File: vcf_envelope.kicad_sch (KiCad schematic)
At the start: 19 parts, among them Q2 BC237, U15 4066, U8 4001, U9 Opamp_Dual

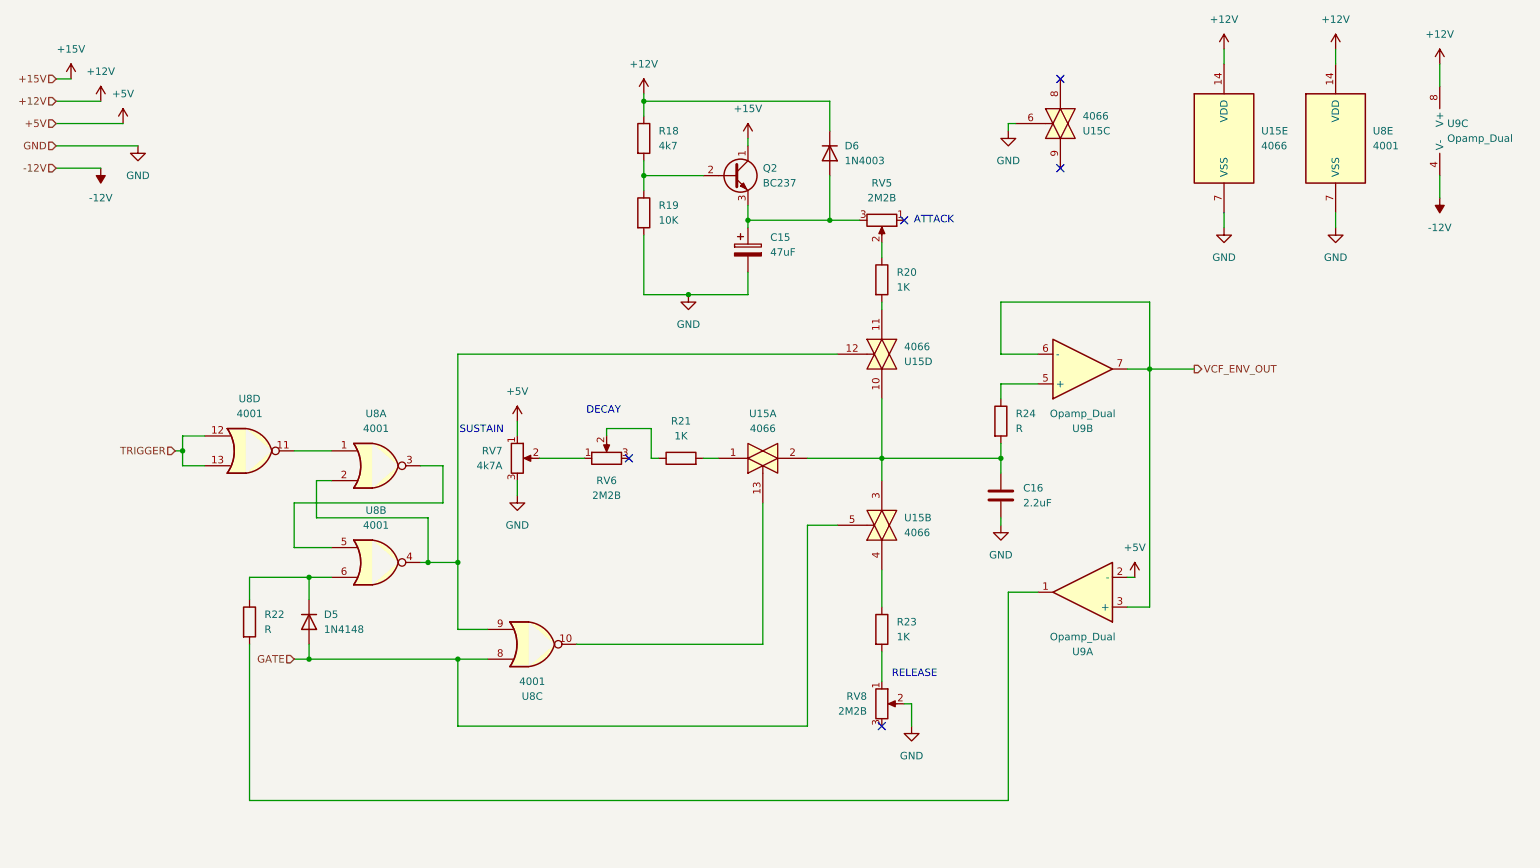
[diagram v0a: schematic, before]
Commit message: Add missing values and connectors
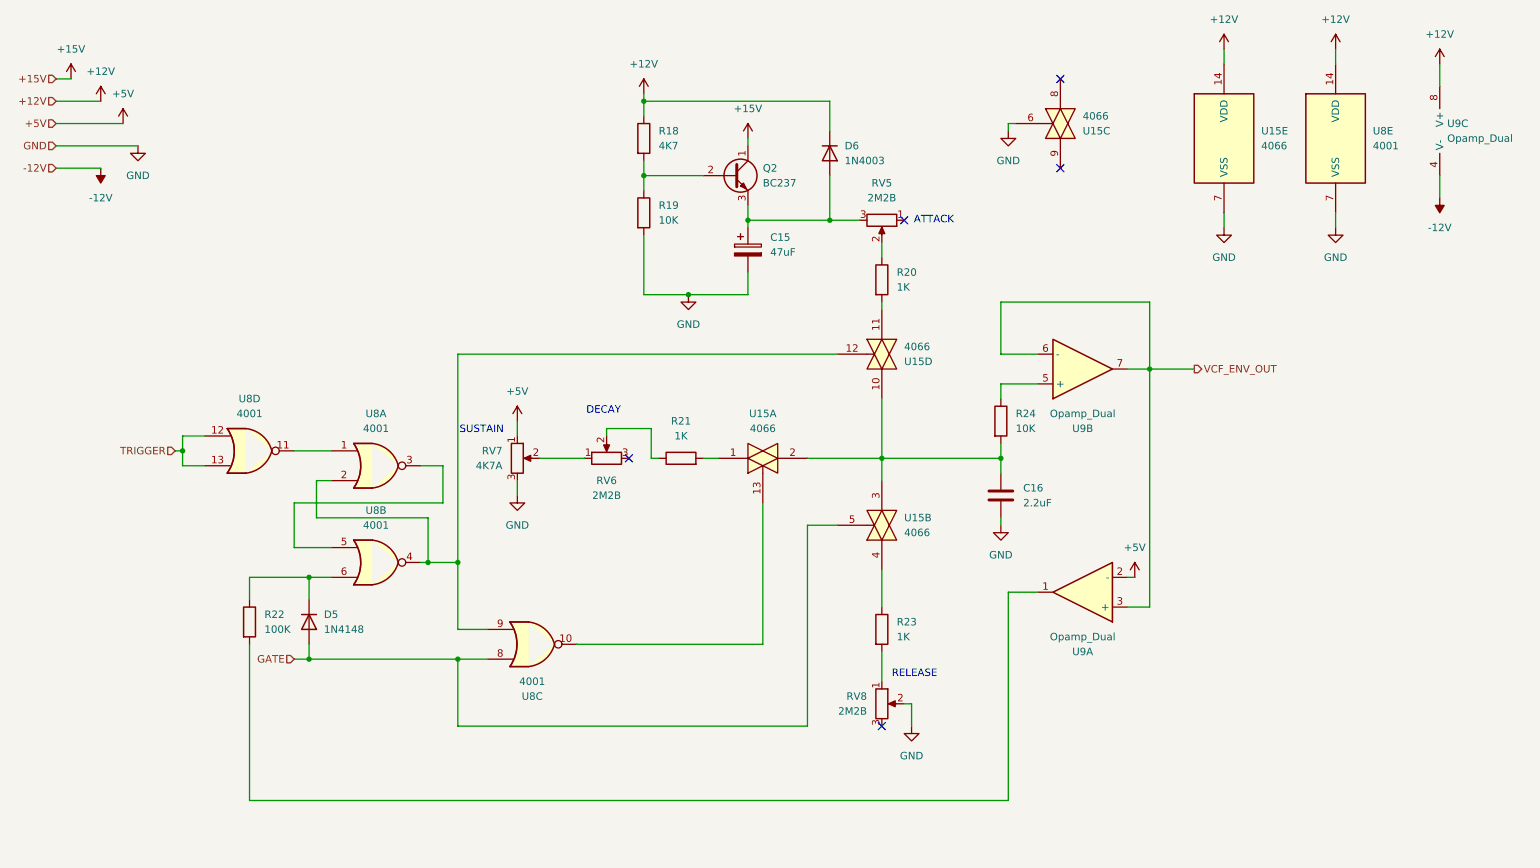
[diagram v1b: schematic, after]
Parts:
- R18: value 4k7 -> 4K7
- R22: value R -> 100K
- R24: value R -> 10K
- RV7: value 4k7A -> 4K7A
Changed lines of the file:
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@@
 			)
 		)
-		(property "Value" "R"
+		(property "Value" "100K"
 			(at 66.04 128.2699 0)
 			(effects
@@
 			)
 		)
-		(property "Value" "4k7"
+		(property "Value" "4K7"
 			(at 133.35 45.7199 0)
 			(effects
@@
 			)
 		)
-		(property "Value" "R"
+		(property "Value" "10K"
 			(at 194.31 93.9799 0)
 			(effects
@@
 			)
 		)
-		(property "Value" "4k7A"
+		(property "Value" "4K7A"
 			(at 106.68 100.3299 0)
 			(effects

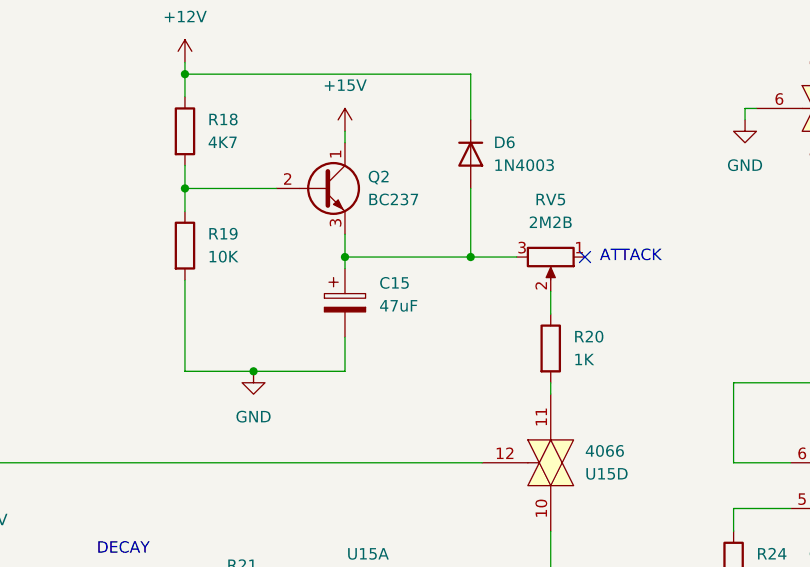
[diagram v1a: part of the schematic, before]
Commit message: Assign footprints and start PCB
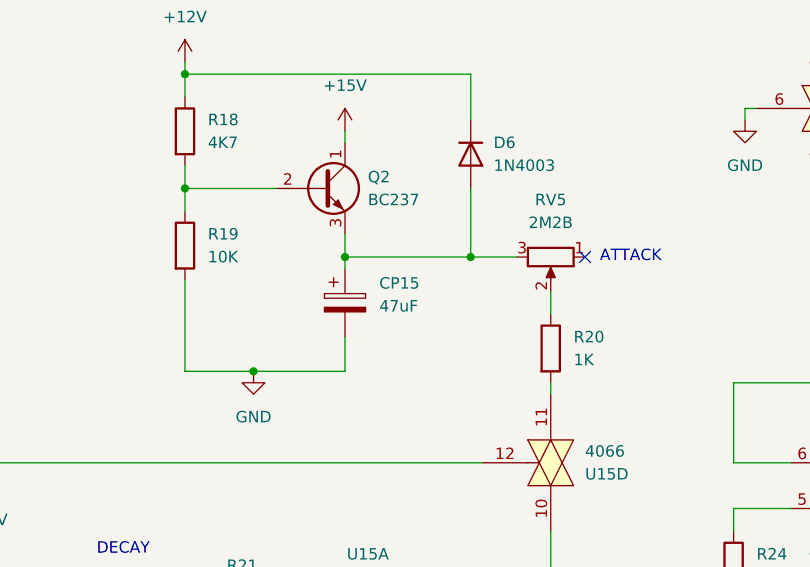
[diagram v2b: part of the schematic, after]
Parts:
- C16: footprint (none) -> Capacitor_THT:C_Disc_D5.0mm_W2.5mm_P5.00mm
- CP15: renamed from C15; footprint (none) -> Capacitor_THT:CP_Radial_D8.0mm_P3.80mm
- R18, R19, R20, R21, R22, R23, R24: footprint (none) -> Resistor_THT:R_Axial_DIN0204_L3.6mm_D1.6mm_P7.62mm_Horizontal
- RV5, RV6, RV7, RV8: footprint (none) -> Potentiometer_THT:Potentiometer_Omeg_PC16BU_Vertical
- U15: footprint (none) -> Package_DIP:DIP-14_W7.62mm_LongPads
- U8: footprint (none) -> Package_DIP:DIP-16_W7.62mm_LongPads
- U9: footprint (none) -> Package_DIP:DIP-8_W7.62mm_LongPads
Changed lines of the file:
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@@
 			)
 		)
-		(property "Footprint" ""
+		(property "Footprint" "Resistor_THT:R_Axial_DIN0204_L3.6mm_D1.6mm_P7.62mm_Horizontal"
 			(at 129.032 57.15 90)
 			(effects
@@
 			)
 		)
-		(property "Footprint" ""
+		(property "Footprint" "Resistor_THT:R_Axial_DIN0204_L3.6mm_D1.6mm_P7.62mm_Horizontal"
 			(at 61.722 127 90)
 			(effects
@@
 			)
 		)
-		(property "Footprint" ""
+		(property "Footprint" "Resistor_THT:R_Axial_DIN0204_L3.6mm_D1.6mm_P7.62mm_Horizontal"
 			(at 129.032 44.45 90)
 			(effects
@@
 			)
 		)
-		(property "Footprint" ""
+		(property "Footprint" "Package_DIP:DIP-8_W7.62mm_LongPads"
 			(at 205.74 83.82 0)
 			(effects
@@
 			)
 		)
-		(property "Footprint" ""
+		(property "Footprint" "Package_DIP:DIP-14_W7.62mm_LongPads"
 			(at 171.45 110.49 0)
 			(effects
@@
 			)
 		)
-		(property "Footprint" ""
+		(property "Footprint" "Package_DIP:DIP-14_W7.62mm_LongPads"
 			(at 201.93 41.91 0)
 			(effects
@@
 			)
 		)
-		(property "Footprint" ""
+		(property "Footprint" "Capacitor_THT:C_Disc_D5.0mm_W2.5mm_P5.00mm"
 			(at 190.8048 101.6 0)
 			(effects
@@
 			)
 		)
-		(property "Footprint" ""
+		(property "Footprint" "Resistor_THT:R_Axial_DIN0204_L3.6mm_D1.6mm_P7.62mm_Horizontal"
 			(at 137.16 100.838 90)
 			(effects
@@
 			)
 		)
-		(property "Footprint" ""
+		(property "Footprint" "Package_DIP:DIP-14_W7.62mm_LongPads"
 			(at 151.13 99.06 0)
 			(effects
@@
 			)
 		)
-		(property "Footprint" ""
+		(property "Footprint" "Potentiometer_THT:Potentiometer_Omeg_PC16BU_Vertical"
 			(at 171.45 58.42 0)
 			(effects
@@
 			)
 		)
-		(property "Footprint" ""
+		(property "Footprint" "Resistor_THT:R_Axial_DIN0204_L3.6mm_D1.6mm_P7.62mm_Horizontal"
 			(at 189.992 92.71 90)
 			(effects
@@
 			)
 		)
-		(property "Footprint" ""
+		(property "Footprint" "Package_DIP:DIP-14_W7.62mm_LongPads"
 			(at 229.87 44.45 0)
 			(effects
@@
 			)
 		)
-		(property "Footprint" ""
+		(property "Footprint" "Potentiometer_THT:Potentiometer_Omeg_PC16BU_Vertical"
 			(at 124.46 99.06 0)
 			(effects
@@
 			)
 		)
-		(property "Footprint" ""
+		(property "Footprint" "Package_DIP:DIP-8_W7.62mm_LongPads"
 			(at 205.74 121.92 0)
 			(effects
@@
 		(dnp no)
 		(fields_autoplaced yes)
-		(property "Reference" "C15"
+		(property "Reference" "CP15"
 			(at 152.4 61.3409 0)
 			(effects
@@
 			)
 		)
-		(property "Footprint" ""
+		(property "Footprint" "Capacitor_THT:CP_Radial_D8.0mm_P3.80mm"
 			(at 149.5552 67.31 0)
 			(effects
@@
 			(project "jensx1000"
 				(path "/3c53febc-5769-4c45-8f8f-0aba2c04e944/0274eb93-a765-4aec-bd65-1454f6ff4ea9"
-					(reference "C15")
+					(reference "CP15")
 					(unit 1)
 				)
@@
 			)
 		)
-		(property "Footprint" ""
+		(property "Footprint" "Package_DIP:DIP-8_W7.62mm_LongPads"
 			(at 269.24 43.18 0)
 			(effects
@@
 			)
 		)
-		(property "Footprint" ""
+		(property "Footprint" "Package_DIP:DIP-16_W7.62mm_LongPads"
 			(at 85.09 100.33 0)
 			(effects
@@
 			)
 		)
-		(property "Footprint" ""
+		(property "Footprint" "Package_DIP:DIP-16_W7.62mm_LongPads"
 			(at 248.92 44.45 0)
 			(effects
@@
 			)
 		)
-		(property "Footprint" ""
+		(property "Footprint" "Package_DIP:DIP-16_W7.62mm_LongPads"
 			(at 63.5 97.79 0)
 			(effects
@@
 			)
 		)
-		(property "Footprint" ""
+		(property "Footprint" "Resistor_THT:R_Axial_DIN0204_L3.6mm_D1.6mm_P7.62mm_Horizontal"
 			(at 169.672 128.27 90)
 			(effects
@@
 			)
 		)
-		(property "Footprint" ""
+		(property "Footprint" "Package_DIP:DIP-14_W7.62mm_LongPads"
 			(at 171.45 81.28 0)
 			(effects
@@
 			)
 		)
-		(property "Footprint" ""
+		(property "Footprint" "Package_DIP:DIP-16_W7.62mm_LongPads"
 			(at 111.76 130.81 0)
 			(effects
@@
 			)
 		)
-		(property "Footprint" ""
+		(property "Footprint" "Resistor_THT:R_Axial_DIN0204_L3.6mm_D1.6mm_P7.62mm_Horizontal"
 			(at 169.672 68.58 90)
 			(effects
@@
 			)
 		)
-		(property "Footprint" ""
+		(property "Footprint" "Potentiometer_THT:Potentiometer_Omeg_PC16BU_Vertical"
 			(at 171.45 140.97 0)
 			(effects
@@
 			)
 		)
-		(property "Footprint" ""
+		(property "Footprint" "Package_DIP:DIP-16_W7.62mm_LongPads"
 			(at 85.09 116.84 0)
 			(effects
@@
 			)
 		)
-		(property "Footprint" ""
+		(property "Footprint" "Potentiometer_THT:Potentiometer_Omeg_PC16BU_Vertical"
 			(at 109.22 99.06 0)
 			(effects

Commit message: VCF components are in position (but PCB size is wrong)
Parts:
- Q2: footprint Package_TO_SOT_THT:TO-92_Inline -> Package_TO_SOT_THT:TO-92_Inline_Wide
- R18, R19, R20, R21, R22, R23, R24: footprint Resistor_THT:R_Axial_DIN0204_L3.6mm_D1.6mm_P7.62mm_Horizontal -> Resistor_THT:R_Axial_DIN0207_L6.3mm_D2.5mm_P15.24mm_Horizontal
- U8: footprint Package_DIP:DIP-16_W7.62mm_LongPads -> Package_DIP:DIP-14_W7.62mm_Socket_LongPads
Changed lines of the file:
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@@
 			)
 		)
-		(property "Footprint" "Resistor_THT:R_Axial_DIN0204_L3.6mm_D1.6mm_P7.62mm_Horizontal"
+		(property "Footprint" "Resistor_THT:R_Axial_DIN0207_L6.3mm_D2.5mm_P15.24mm_Horizontal"
 			(at 129.032 57.15 90)
 			(effects
@@
 			)
 		)
-		(property "Footprint" "Resistor_THT:R_Axial_DIN0204_L3.6mm_D1.6mm_P7.62mm_Horizontal"
+		(property "Footprint" "Resistor_THT:R_Axial_DIN0207_L6.3mm_D2.5mm_P15.24mm_Horizontal"
 			(at 61.722 127 90)
 			(effects
@@
 			)
 		)
-		(property "Footprint" "Resistor_THT:R_Axial_DIN0204_L3.6mm_D1.6mm_P7.62mm_Horizontal"
+		(property "Footprint" "Resistor_THT:R_Axial_DIN0207_L6.3mm_D2.5mm_P15.24mm_Horizontal"
 			(at 129.032 44.45 90)
 			(effects
@@
 			)
 		)
-		(property "Footprint" "Resistor_THT:R_Axial_DIN0204_L3.6mm_D1.6mm_P7.62mm_Horizontal"
+		(property "Footprint" "Resistor_THT:R_Axial_DIN0207_L6.3mm_D2.5mm_P15.24mm_Horizontal"
 			(at 137.16 100.838 90)
 			(effects
@@
 			)
 		)
-		(property "Footprint" "Resistor_THT:R_Axial_DIN0204_L3.6mm_D1.6mm_P7.62mm_Horizontal"
+		(property "Footprint" "Resistor_THT:R_Axial_DIN0207_L6.3mm_D2.5mm_P15.24mm_Horizontal"
 			(at 189.992 92.71 90)
 			(effects
@@
 			)
 		)
-		(property "Footprint" "Package_DIP:DIP-16_W7.62mm_LongPads"
+		(property "Footprint" "Package_DIP:DIP-14_W7.62mm_Socket_LongPads"
 			(at 85.09 100.33 0)
 			(effects
@@
 			)
 		)
-		(property "Footprint" "Package_DIP:DIP-16_W7.62mm_LongPads"
+		(property "Footprint" "Package_DIP:DIP-14_W7.62mm_Socket_LongPads"
 			(at 248.92 44.45 0)
 			(effects
@@
 			)
 		)
-		(property "Footprint" "Package_DIP:DIP-16_W7.62mm_LongPads"
+		(property "Footprint" "Package_DIP:DIP-14_W7.62mm_Socket_LongPads"
 			(at 63.5 97.79 0)
 			(effects
@@
 			)
 		)
-		(property "Footprint" "Resistor_THT:R_Axial_DIN0204_L3.6mm_D1.6mm_P7.62mm_Horizontal"
+		(property "Footprint" "Resistor_THT:R_Axial_DIN0207_L6.3mm_D2.5mm_P15.24mm_Horizontal"
 			(at 169.672 128.27 90)
 			(effects
@@
 			)
 		)
-		(property "Footprint" "Package_DIP:DIP-16_W7.62mm_LongPads"
+		(property "Footprint" "Package_DIP:DIP-14_W7.62mm_Socket_LongPads"
 			(at 111.76 130.81 0)
 			(effects
@@
 			)
 		)
-		(property "Footprint" "Resistor_THT:R_Axial_DIN0204_L3.6mm_D1.6mm_P7.62mm_Horizontal"
+		(property "Footprint" "Resistor_THT:R_Axial_DIN0207_L6.3mm_D2.5mm_P15.24mm_Horizontal"
 			(at 169.672 68.58 90)
 			(effects
@@
 			)
 		)
-		(property "Footprint" "Package_DIP:DIP-16_W7.62mm_LongPads"
+		(property "Footprint" "Package_DIP:DIP-14_W7.62mm_Socket_LongPads"
 			(at 85.09 116.84 0)
 			(effects
@@
 			)
 		)
-		(property "Footprint" "Package_TO_SOT_THT:TO-92_Inline"
+		(property "Footprint" "Package_TO_SOT_THT:TO-92_Inline_Wide"
 			(at 151.13 52.705 0)
 			(effects

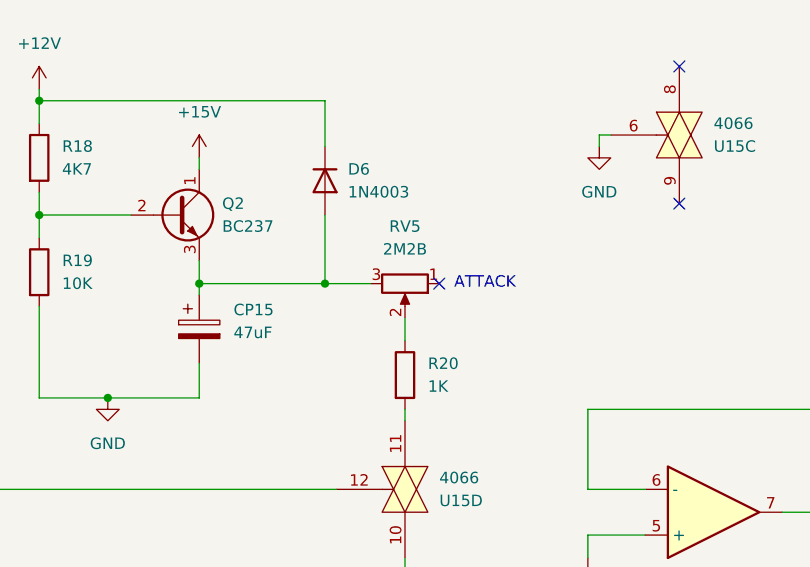
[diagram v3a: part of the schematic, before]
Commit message: Fix PCB sizes, adjust layout to new size
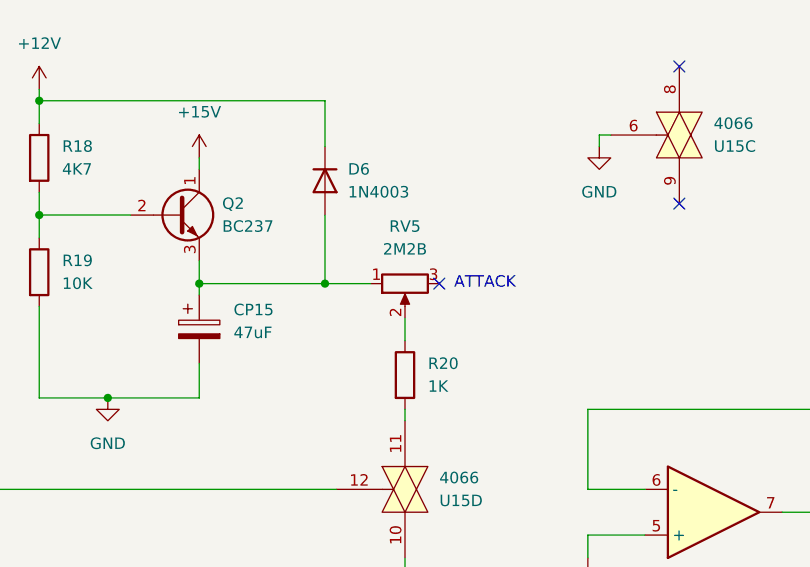
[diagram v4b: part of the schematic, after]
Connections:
- net at RV5.1: now also CP15.1, D6.2 (A), Q2.3 (E)
- now unconnected: RV5.3
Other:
- moved on the sheet: RV5
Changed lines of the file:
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@@
 	(symbol
 		(lib_id "Device:R_Potentiometer")
-		(at 171.45 58.42 270)
+		(at 171.45 58.42 90)
+		(mirror x)
 		(unit 1)
 		(exclude_from_sim no)
@@
 		(on_board yes)
 		(dnp no)
-		(fields_autoplaced yes)
 		(property "Reference" "RV5"
 			(at 171.45 52.07 90)

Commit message: Routing
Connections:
- net GND: now also R23.2; no longer RV8.2
- net at U15.4: now also RV8.1; no longer R23.1
- new net: R23.1, RV8.2
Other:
- moved on the sheet: R23, RV8
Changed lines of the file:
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@@
 	(text "RELEASE"
 		(exclude_from_sim no)
-		(at 177.038 135.89 0)
+		(at 166.624 134.366 0)
 		(effects
 			(font
@@
 	)
 	(junction
+		(at 176.53 140.97)
+		(diameter 0)
+		(color 0 0 0 0)
+	)
+	(junction
 		(at 52.07 97.79)
 		(diameter 0)
@@
 	)
 	(no_connect
-		(at 171.45 144.78)
+		(at 171.45 132.08)
 	)
 	(no_connect
@@
 	(wire
 		(pts
+			(xy 176.53 128.27) (xy 175.26 128.27)
+		)
+		(stroke
+			(width 0)
+			(type default)
+		)
+	)
+	(wire
+		(pts
 			(xy 158.75 99.06) (xy 171.45 99.06)
 		)
@@
 	(wire
 		(pts
-			(xy 171.45 132.08) (xy 171.45 137.16)
-		)
-		(stroke
-			(width 0)
-			(type default)
-		)
-	)
-	(wire
-		(pts
 			(xy 171.45 99.06) (xy 171.45 102.87)
 		)
@@
 	(wire
 		(pts
+			(xy 176.53 133.35) (xy 176.53 128.27)
+		)
+		(stroke
+			(width 0)
+			(type default)
+		)
+	)
+	(wire
+		(pts
 			(xy 71.12 133.35) (xy 73.66 133.35)
 		)
@@
 	(symbol
 		(lib_id "Device:R")
-		(at 171.45 128.27 0)
+		(at 176.53 137.16 0)
 		(unit 1)
 		(exclude_from_sim no)
@@
 		(fields_autoplaced yes)
 		(property "Reference" "R23"
-			(at 173.99 126.9999 0)
+			(at 179.07 135.8899 0)
 			(effects
 				(font
@@
 		)
 		(property "Value" "1K"
-			(at 173.99 129.5399 0)
+			(at 179.07 138.4299 0)
 			(effects
 				(font
@@
 		)
 		(property "Footprint" "Resistor_THT:R_Axial_DIN0207_L6.3mm_D2.5mm_P15.24mm_Horizontal"
-			(at 169.672 128.27 90)
+			(at 174.752 137.16 90)
 			(effects
 				(font
@@
 		)
 		(property "Datasheet" "~"
-			(at 171.45 128.27 0)
+			(at 176.53 137.16 0)
 			(effects
 				(font
@@
 		)
 		(property "Description" "Resistor"
-			(at 171.45 128.27 0)
+			(at 176.53 137.16 0)
 			(effects
 				(font
@@
 	(symbol
 		(lib_id "Device:R_Potentiometer")
-		(at 171.45 140.97 0)
+		(at 171.45 128.27 0)
 		(unit 1)
 		(exclude_from_sim no)
@@
 		(fields_autoplaced yes)
 		(property "Reference" "RV8"
-			(at 168.91 139.6999 0)
+			(at 168.91 126.9999 0)
 			(effects
 				(font
@@
 		)
 		(property "Value" "2M2B"
-			(at 168.91 142.2399 0)
+			(at 168.91 129.5399 0)
 			(effects
 				(font
@@
 		)
 		(property "Footprint" "Potentiometer_THT:Potentiometer_Omeg_PC16BU_Vertical"
-			(at 171.45 140.97 0)
+			(at 171.45 128.27 0)
 			(effects
 				(font
@@
 		)
 		(property "Datasheet" "~"
-			(at 171.45 140.97 0)
+			(at 171.45 128.27 0)
 			(effects
 				(font
@@
 		)
 		(property "Description" "Potentiometer"
-			(at 171.45 140.97 0)
+			(at 171.45 128.27 0)
 			(effects
 				(font

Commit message: Routing
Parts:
- C16: footprint Capacitor_THT:C_Disc_D5.0mm_W2.5mm_P5.00mm -> Capacitor_THT:C_Rect_L16.5mm_W4.7mm_P15.00mm_MKT
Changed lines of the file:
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@@
 			)
 		)
-		(property "Footprint" "Capacitor_THT:C_Disc_D5.0mm_W2.5mm_P5.00mm"
+		(property "Footprint" "Capacitor_THT:C_Rect_L16.5mm_W4.7mm_P15.00mm_MKT"
 			(at 190.8048 101.6 0)
 			(effects

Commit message: Routing
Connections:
- net +5V: now also RV7.3; no longer RV7.1
- net GND: now also RV7.1; no longer RV7.3
- net LFO_OUT: now reaches R22.2, U9.1
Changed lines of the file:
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@@
 	(wire
 		(pts
+			(xy 71.12 137.16) (xy 73.66 137.16)
+		)
+		(stroke
+			(width 0)
+			(type default)
+		)
+	)
+	(wire
+		(pts
 			(xy 99.06 116.84) (xy 99.06 128.27)
 		)
@@
 		)
 	)
+	(wire
+		(pts
+			(xy 73.66 137.16) (xy 73.66 133.35)
+		)
+		(stroke
+			(width 0)
+			(type default)
+		)
+	)
+	(label "TRIGGER"
+		(at 52.07 95.25 180)
+		(effects
+			(font
+				(size 1.27 1.27)
+			)
+			(justify right bottom)
+		)
+	)
+	(label "GATE"
+		(at 71.12 137.16 180)
+		(effects
+			(font
+				(size 1.27 1.27)
+			)
+			(justify right bottom)
+		)
+	)
+	(label "LFO_OUT"
+		(at 162.56 157.48 270)
+		(effects
+			(font
+				(size 1.27 1.27)
+			)
+			(justify right bottom)
+		)
+	)
 	(hierarchical_label "VCF_ENV_OUT"
 		(shape output)
@@
 		(lib_id "Device:R_Potentiometer")
 		(at 109.22 99.06 0)
+		(mirror x)
 		(unit 1)
 		(exclude_from_sim no)
